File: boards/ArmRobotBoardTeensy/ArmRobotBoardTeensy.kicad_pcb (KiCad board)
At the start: 2 copper layers, 87.5 x 55 mm, 49 parts, among them J1 B5B-XH-A, J10 B4B-XH-A, J11 B3B-XH-A, J2 B4B-XH-A, J3 B3B-XH-A, J4 B3B-XH-A, J5 B4B-XH-A, J6 B2B-XH-A, J7 B2B-XH-A, J8 B4B-XH-A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

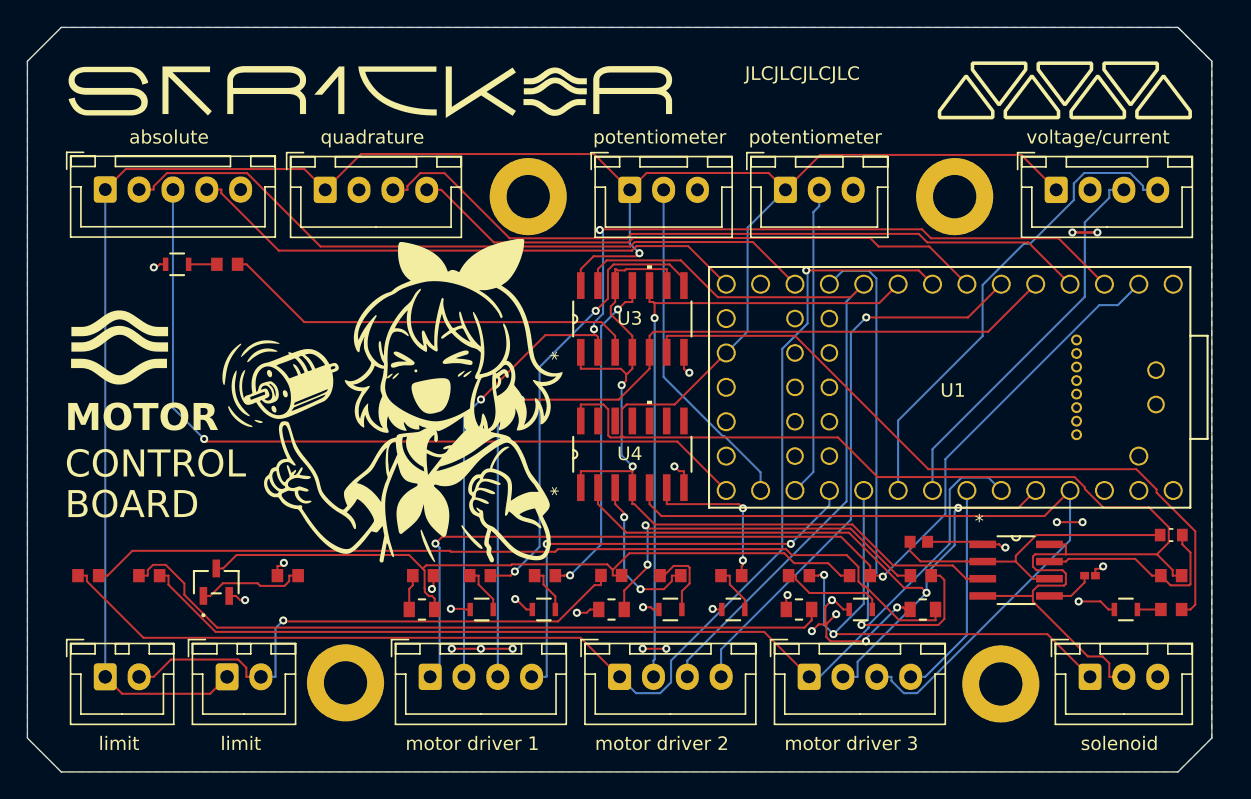
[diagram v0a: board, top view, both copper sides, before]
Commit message: Fixed LED footprint and re-exported
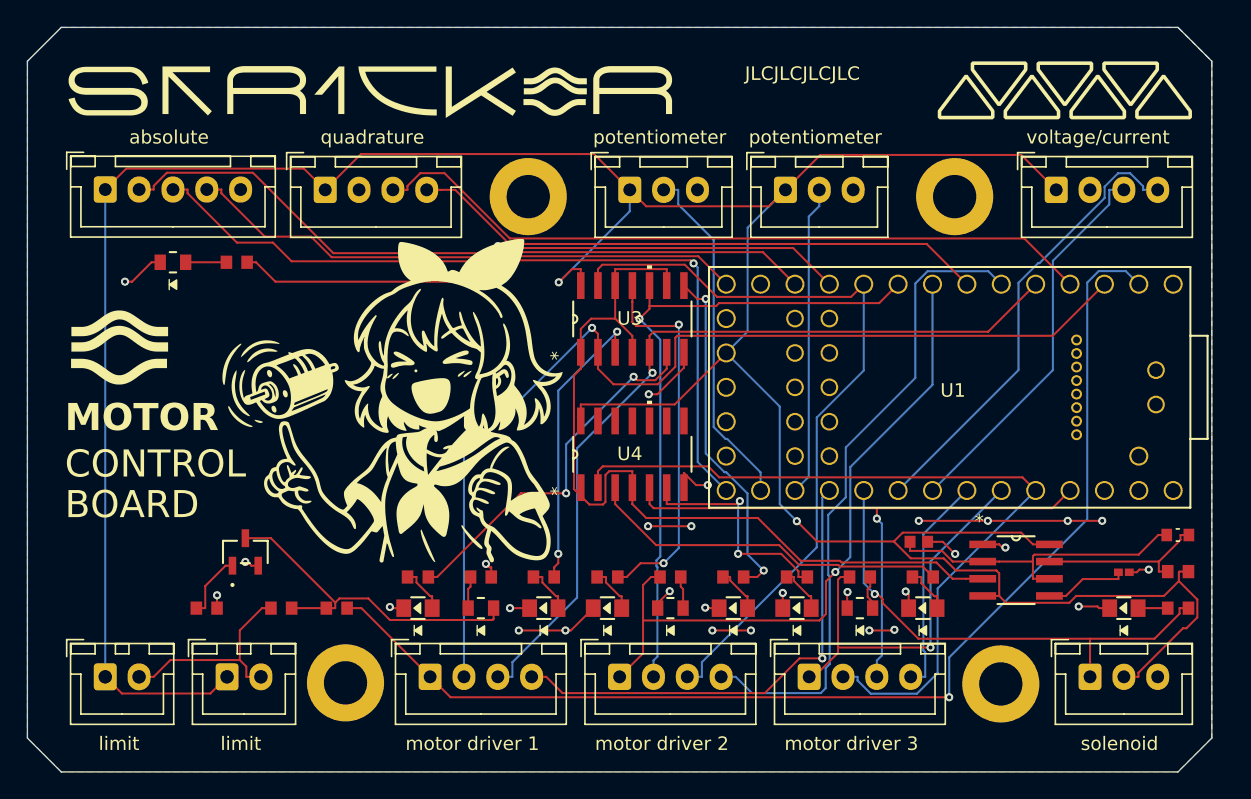
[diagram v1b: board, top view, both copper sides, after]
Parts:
- D1, D2, D3, D4, D6, D7, D9: footprint 150080BS75000:150080BS75000 -> 150080BS75000:150080BS75000_Modified
- D10, D11, D5, D8: footprint LED_XL-2012:LED_XL-2012SURC_XLG -> XL-2012UPC:LED_XL-2012SURC_XLG
- moved R2 55.7 mm to (128.9, 114.6)
- moved R10 55.6 mm to (115.5, 91.3)
- moved R13 52.5 mm to (161.5, 114.6), turned to 180 degrees
- moved D2 52.3 mm to (128.9, 116.9)
- moved R12 43.0 mm to (147.5, 114.6)
- moved D8 41.3 mm to (110.8, 91.3)
- moved R9 38.7 mm to (122.8, 116.9)
- moved D1 37.1 mm to (138.1, 116.9)
- moved R1 32.9 mm to (138.1, 114.6)
- moved R11 28.1 mm to (185.0, 116.9)
- moved R8 24.5 mm to (118.8, 116.9)
- moved D9 19.4 mm to (181.0, 116.9)
- moved R3 18.7 mm to (152.1, 114.6)
- moved D10 18.6 mm to (147.5, 116.9)
- moved D6 18.6 mm to (166.1, 116.9)
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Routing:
- net Net-(D10-Pad2): track 66.3 -> 2.37 mm
- net Net-(D11-Pad2): track 53.7 -> 2.53 mm
- net PWM3EN: track 74.6 -> 29.8 mm, vias 0 -> 1
- net PWM2EN: track 92.4 -> 50.3 mm
- net Net-(Q1-COLLECTOR): track 53.7 -> 25.6 mm
- net Net-(J6-Pin_2): track 41.3 -> 15.6 mm, vias 1 -> 0
- net LPWM1A: track 53.0 -> 27.5 mm, vias 0 -> 2
- net Net-(D8-Pad2): track 28.1 -> 3.01 mm, vias 2 -> 0
- net RPWM3A: track 11.9 -> 26.9 mm, vias 2 -> 0
- net PWM1EN: track 75.4 -> 86.6 mm, vias 2 -> 1
- net +3.3V: track 246.1 -> 234.9 mm, vias 1 -> 2
- net LPWM3: track 56.7 -> 45.7 mm, vias 0 -> 1
- net GND: track 48.4 -> 58.7 mm
- net RPWM1A: track 31.3 -> 21.6 mm, vias 0 -> 2
- net RPWM2A: track 33.8 -> 25.6 mm
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
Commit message: Correct missing connections and two LED resistors because LEDs were too dim
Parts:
- R1, R11, R2, R3, R4, R6, R7: value 1K -> 150R
- R10, R12, R13, R5: value 1K -> 470R; footprint RCG06031K00FKEA:RCG06031K00FKEA -> RC0603FR-07470RL:RC0603FR-07470RL
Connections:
- net Net-(J6-Pin_2) renamed /PWM1EN_LIMIT_KILL
- D5 pad 2: Net-(Q1-COLLECTOR) -> PWM1EN
- Q1 pad 3: Net-(Q1-COLLECTOR) -> PWM1EN
- R8 pad 2: Net-(Q1-COLLECTOR) -> Net-(Q1-BASE)
- R9 pad 1: Net-(Q1-COLLECTOR) -> PWM1EN
- R9 pad 2: PWM1EN -> PWM1ENSIG
- U1 pad 2: PWM1EN -> PWM1ENSIG
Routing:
- net PWM1ENSIG: track 0.00 -> 71.6 mm, vias 0 -> 2
- net PWM1EN: track 86.6 -> 26.3 mm, vias 1 -> 0
- net LPWM3: track 45.7 -> 94.8 mm, vias 1 -> 0
- net BLINK: track 64.8 -> 99.7 mm
- net Net-(Q1-COLLECTOR): track 25.6 -> 0.00 mm
- net RPWM3A: track 26.9 -> 42.8 mm
- net A: track 54.1 -> 63.5 mm
- net LPWM1A: track 27.5 -> 35.4 mm
- net +3.3V: track 234.9 -> 242.3 mm
- net Net-(Q1-BASE): track 4.92 -> 10.5 mm
- net LPWM2A: track 28.2 -> 22.6 mm
- net PWM3EN: track 29.8 -> 24.9 mm, vias 1 -> 2
- net GND: track 58.7 -> 53.9 mm, vias 29 -> 32
- net PWM2VT: track 48.2 -> 43.6 mm
- net SCK: track 58.7 -> 55.2 mm
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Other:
- board text removed: "JLCJLCJLCJLC"

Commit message: Fix hi-z (floating) pins for solenoid and PWM channel 1
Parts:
- added R17: 100K, CRCW0603100KFKEA:CRCW0603100KFKEA, F.Cu at (177.9, 117.4)
- R9: value 1K -> 100K; footprint RCG06031K00FKEA:RCG06031K00FKEA -> CRCW0603100KFKEA:CRCW0603100KFKEA
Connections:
- R9 pad 1: PWM1EN -> GND
- R9 pad 2: PWM1ENSIG -> PWM1EN
- U1 pad 2: PWM1ENSIG -> PWM1EN
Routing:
- net PWM1ENSIG: track 71.6 -> 0.00 mm, vias 2 -> 0
- net PWM1EN: track 26.3 -> 96.5 mm, vias 0 -> 2
- net GND: track 53.9 -> 57.4 mm, vias 32 -> 33
- net SIG: track 38.7 -> 40.0 mm
